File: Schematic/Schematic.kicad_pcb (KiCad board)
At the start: 2 copper layers, 115.1 x 171.2 mm, 126 parts, among them J1 HUB75_DATA, J10 Conn_01x03_Pin, J11 Conn_01x03_Pin, J12 Conn_01x03_Pin, J17 Conn_01x03_Pin, J18 LASER, J19 LDR, J2 KEYPAD, J20 WS2812B_DATA, J21 WS2812B_PWR, J3 HUB75_PWR, J4 AUDIO_OUT, J5 DEBUG_HEADER, J6 Conn_01x03_Pin, J7 Conn_01x03_Pin, J8 Conn_01x03_Pin, J9 Conn_01x03_Pin, SW1 RESET, U1 74LS08, U2 STM32F091RCT6, U3 LM386, U4 LM2678S-12, U5 LD1117S33TR_SOT223, U6 MAX7375AXR805, U7 LM358

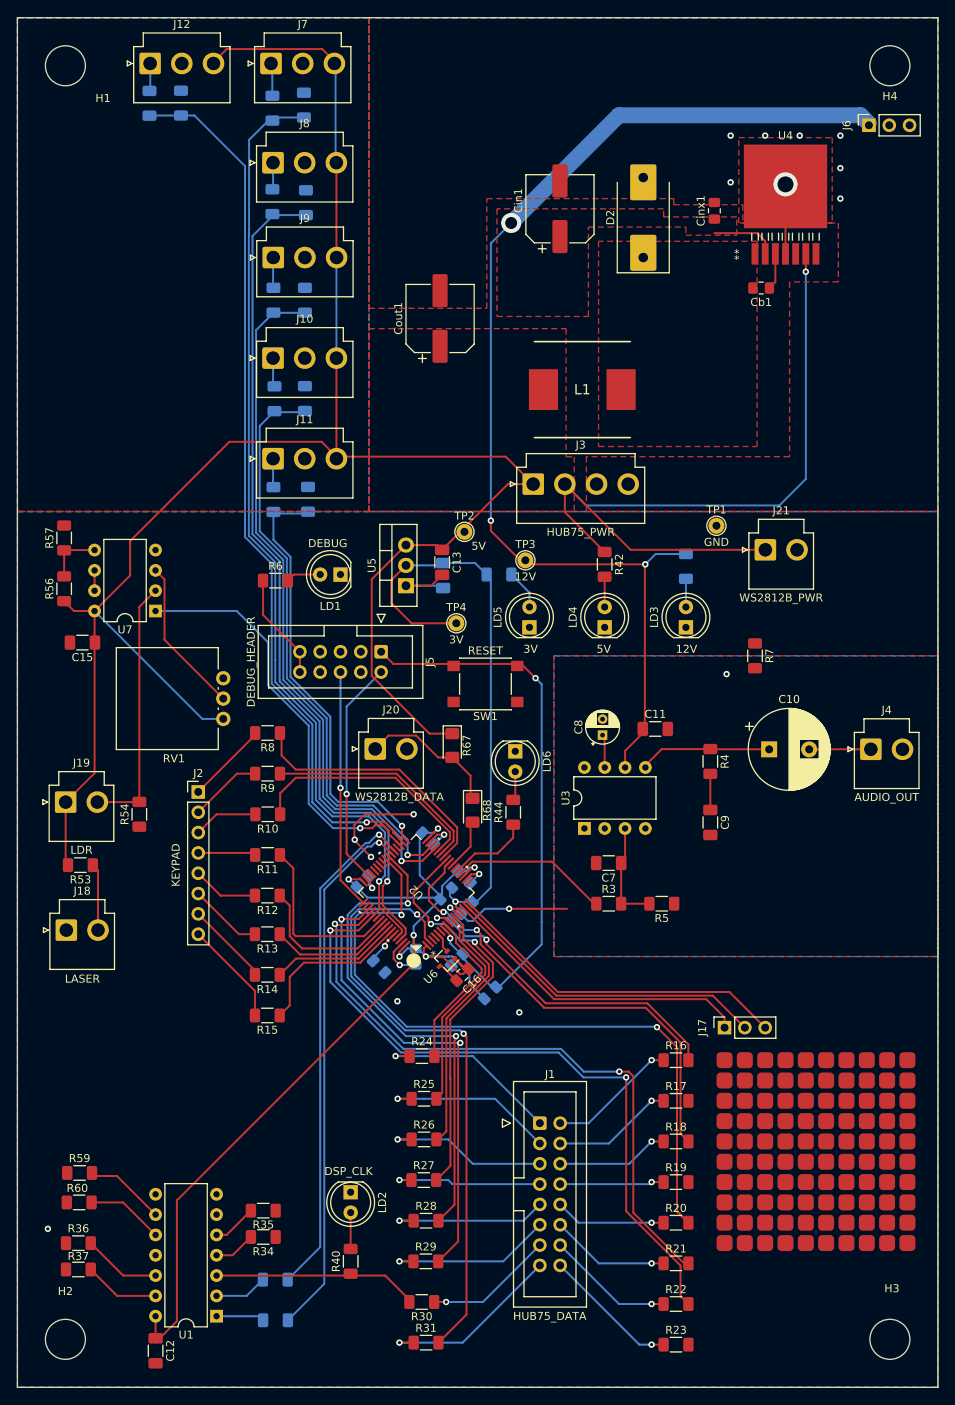
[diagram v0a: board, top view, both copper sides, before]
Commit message: fixed exporting script
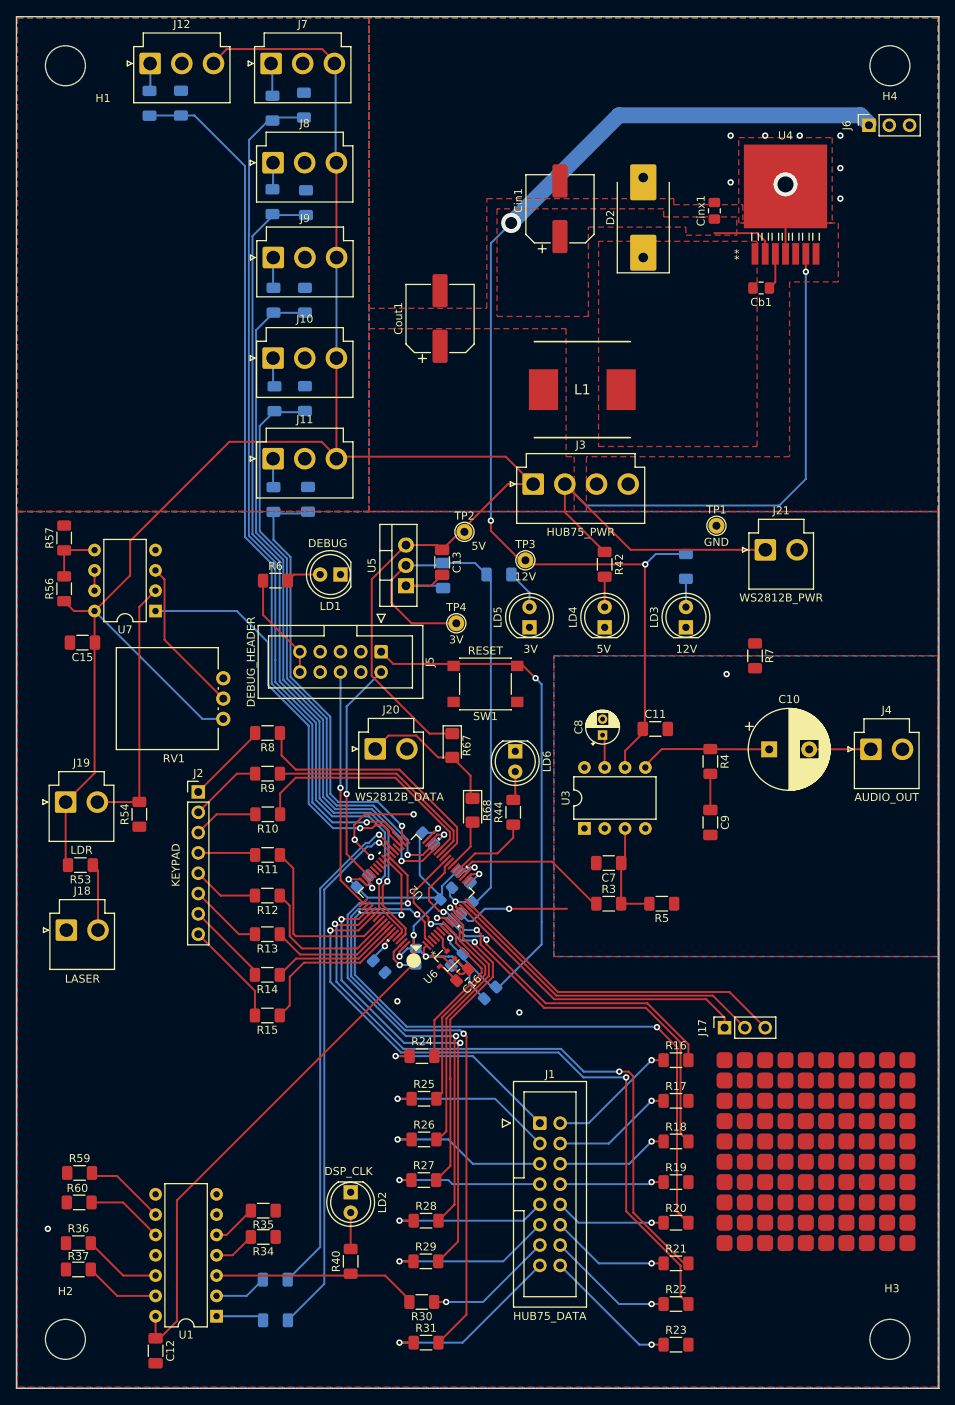
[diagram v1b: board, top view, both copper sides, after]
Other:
- board size 115.1 x 171.2 mm -> 115.3 x 171.4 mm
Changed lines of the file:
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@@
     (aux_axis_origin 35.941 23.622)
     (pcbplotparams
-      (layerselection 0x0011010_fffffffe)
+      (layerselection 0x0000000_fffffffe)
       (plot_on_all_layers_selection 0x0011010_80000000)
       (disableapertmacros false)
@@
       (plotreference true)
       (plotvalue true)
-      (plotinvisibletext false)
+      (plotinvisibletext true)
       (sketchpadsonfab false)
       (subtractmaskfromsilk false)
@@
   (gr_circle (center 151.003 23.622) (end 151.003 23.622)
     (stroke (width 0.15) (type default)) (fill none) (layer "Dwgs.User"))
-  (gr_circle (center 35.941 23.622) (end 36.068 23.622)
+  (gr_circle (center 35.941 23.622) (end 35.941 23.622)
     (stroke (width 0.15) (type default)) (fill none) (layer "Dwgs.User"))
-  (gr_rect (start 35.941 23.622) (end 151.003 194.818)
+  (gr_rect (start 35.814 23.495) (end 151.13 194.945)
     (stroke (width 0.1) (type default)) (fill none) (layer "Edge.Cuts"))
   (gr_text "12V" (at 118.237 103.124) (layer "F.SilkS")

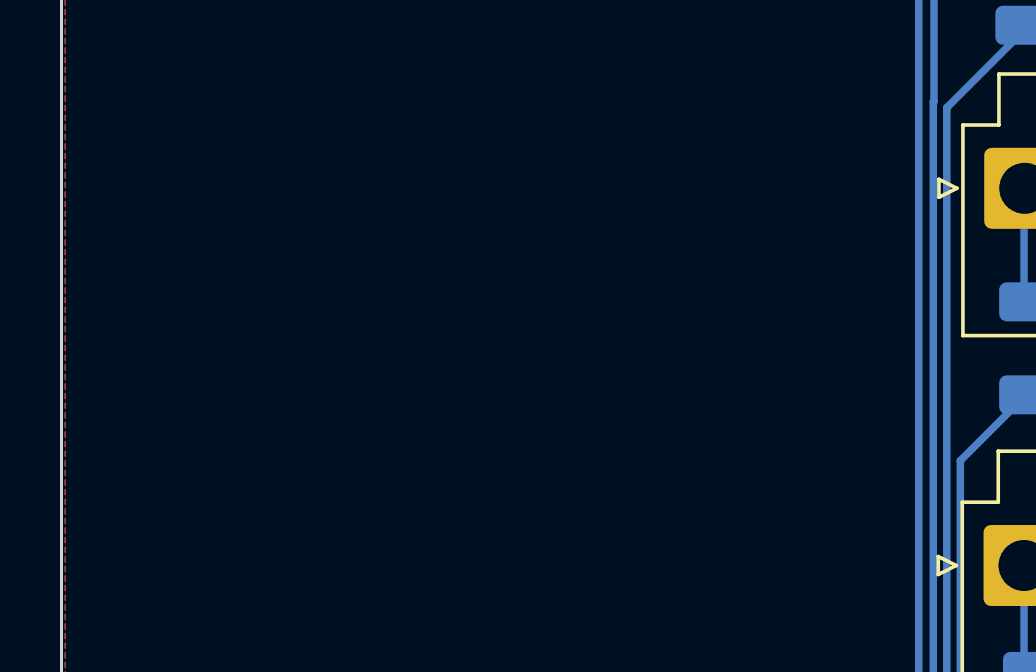
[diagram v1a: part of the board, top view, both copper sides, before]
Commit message: Updated svg's
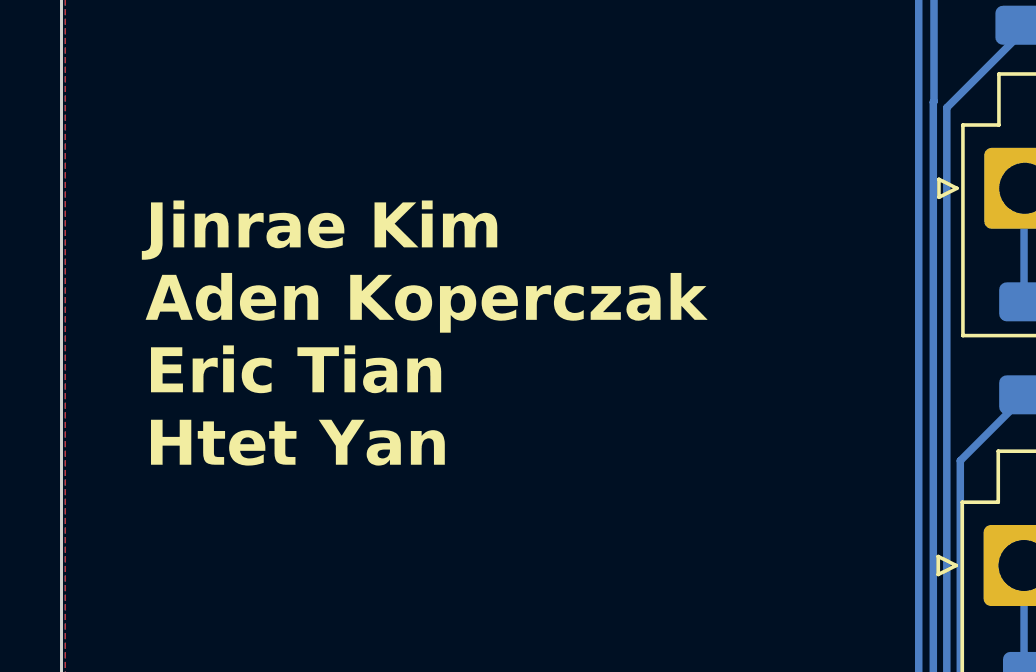
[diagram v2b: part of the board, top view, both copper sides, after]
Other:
- board text added: "Jinrae Kim​ Aden Koperczak​ Eric Tian​ Htet Yan​"
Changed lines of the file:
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@@
   (gr_rect (start 35.814 23.495) (end 151.13 194.945)
     (stroke (width 0.1) (type default)) (fill none) (layer "Edge.Cuts"))
+  (gr_text "Jinrae Kim​\nAden Koperczak​\nEric Tian​\nHtet Yan​" (at 38.608 62.992) (layer "F.SilkS")
+    (effects (font (size 1.5 1.5) (thickness 0.3) bold) (justify left bottom))
+  )
   (gr_text "12V" (at 118.237 103.124) (layer "F.SilkS")
     (effects (font (size 1 1) (thickness 0.15)) (justify left bottom))

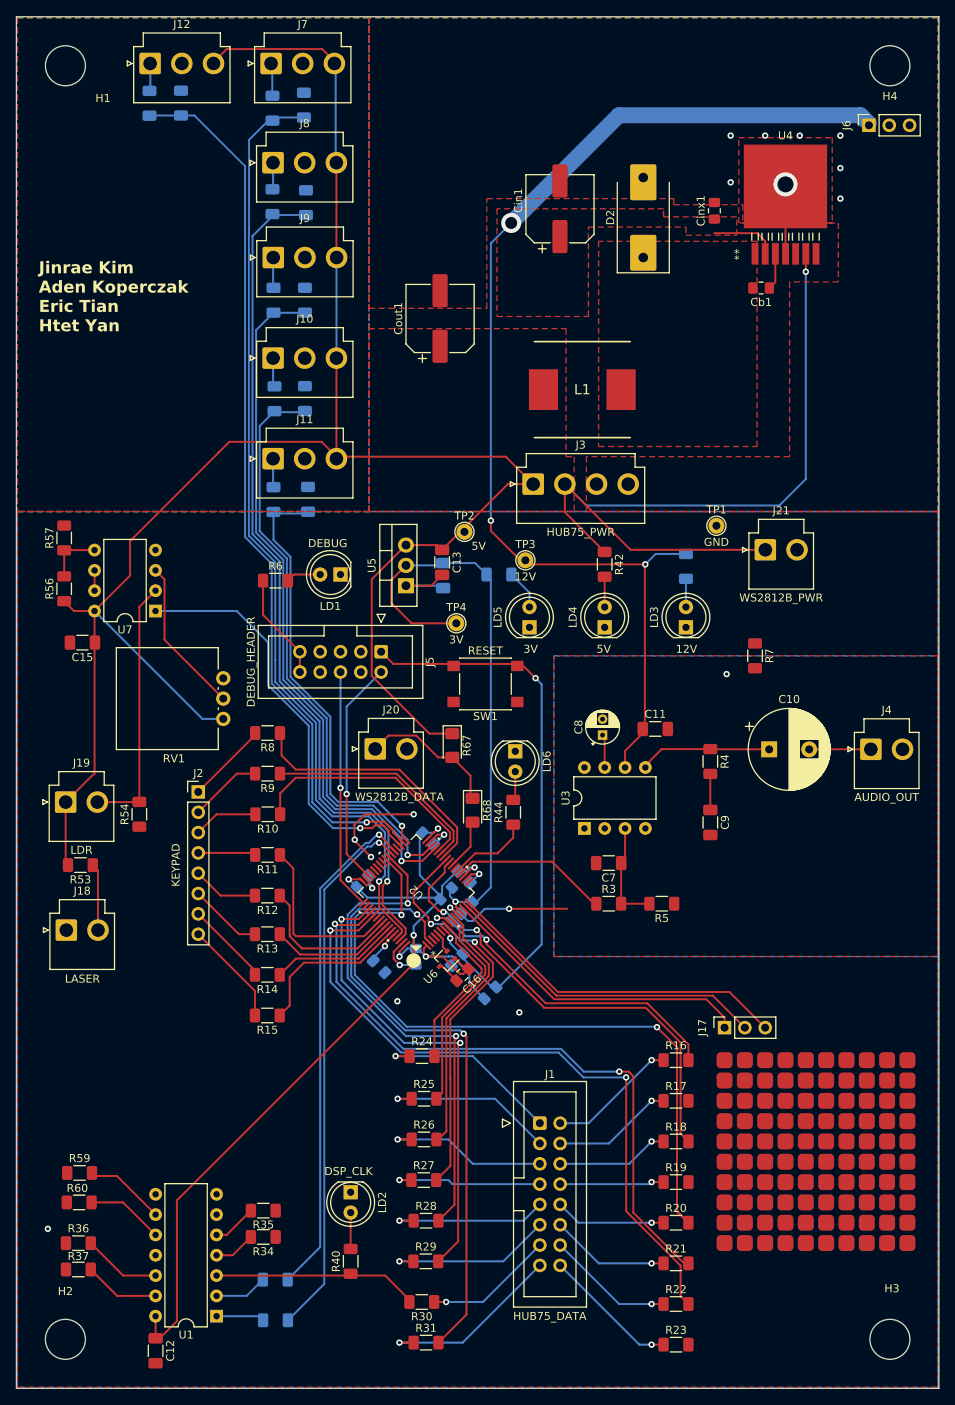
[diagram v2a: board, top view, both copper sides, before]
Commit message: Implemented some suggestions from presentation. Power trace size, reset button position, mounting holes, copper fill near edge, WS Data moved, removed debuge LED and analog vias.
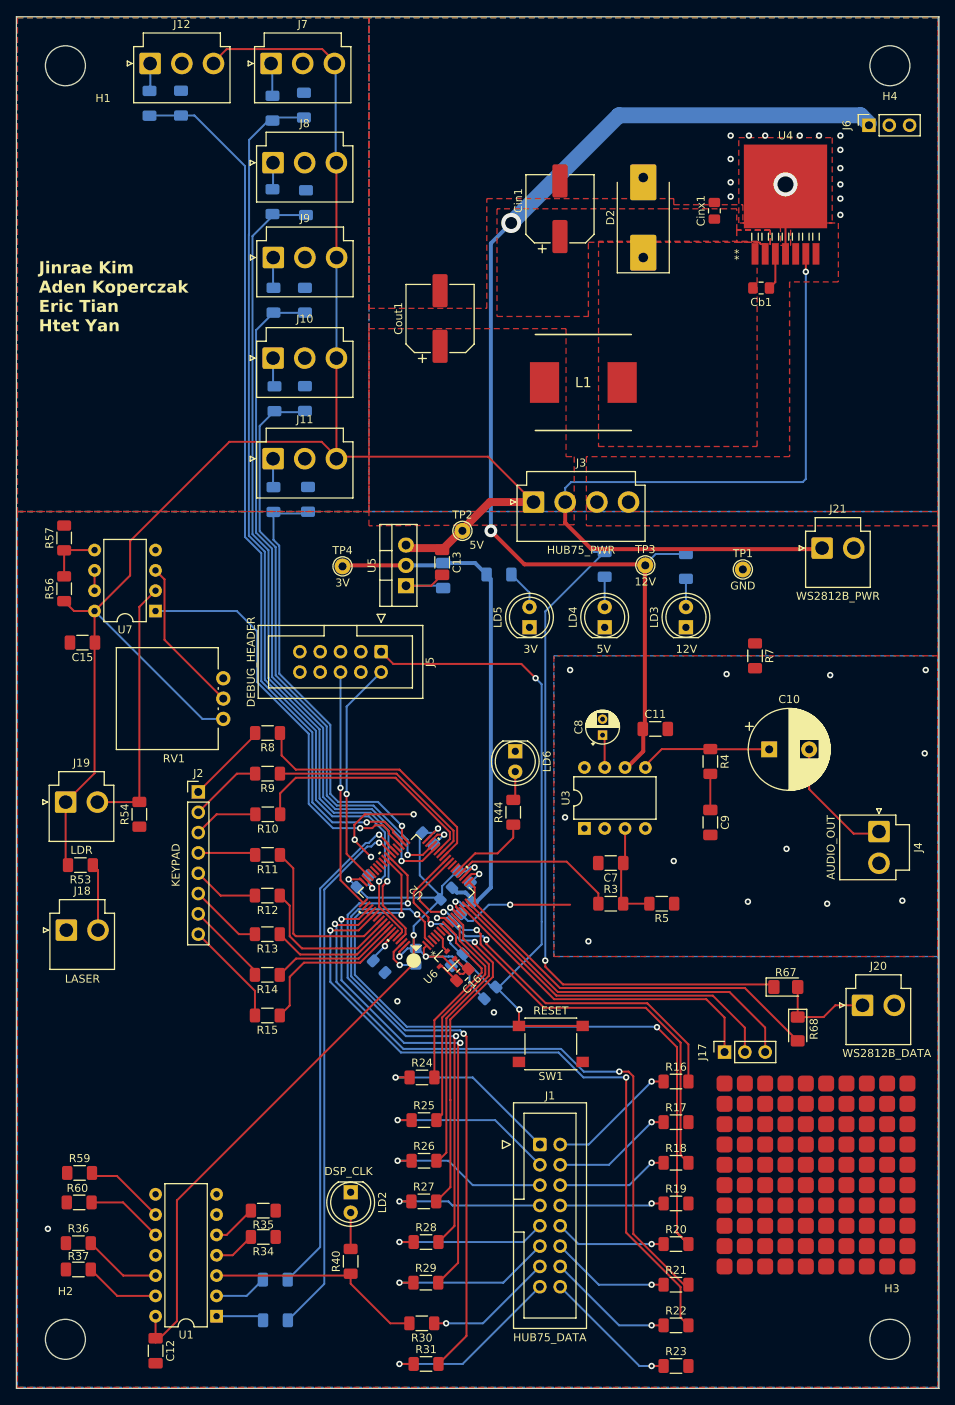
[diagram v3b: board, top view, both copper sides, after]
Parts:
- removed LD1: LED_Red, LED_THT:LED_D5.0mm
- removed R6: 10k, Resistor_SMD:R_1206_3216Metric_Pad1.30x1.75mm_HandSolder
- R42: moved to B.Cu
- moved J20 68.8 mm to (141.6, 147.1)
- moved R67 51.5 mm to (132.0, 144.8), turned to 0 degrees
- moved R68 49.0 mm to (133.5, 150.0)
- moved SW1 45.7 mm to (102.6, 151.9)
- moved TP4 15.9 mm to (76.6, 92.2)
- moved TP3 15.0 mm to (114.4, 92.1)
- moved J4 10.3 mm to (143.6, 125.3), turned to -90 degrees
- moved J21 7.09 mm to (136.5, 89.9)
- moved TP1 6.38 mm to (126.6, 92.6)
- moved J17 3.05 mm to (124.3, 152.9)
- moved REF** 2.92 mm to (124.3, 156.8)
- moved J1 2.67 mm to (101.2, 164.5)
- moved R16 2.67 mm to (118.3, 156.6)
- moved R17 2.67 mm to (118.3, 161.7)
- moved R18 2.67 mm to (118.3, 166.8)
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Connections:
- J5 pad 10: /microprocessor/U5V -> unconnected-(J5-Pin_10-Pad10)
- R68 pad 2: PA7 -> PA3
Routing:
- net +5V: track 343.6 -> 403.0 mm, vias 1 -> 2
- net PA3: track 0.00 -> 50.4 mm
- net /microprocessor/NRST: track 72.6 -> 86.7 mm, vias 2 -> 3
- net /microprocessor/U5V: track 13.3 -> 0.00 mm
- net +12V: track 151.7 -> 143.5 mm, vias 3 -> 2
- net Net-(J4-Pin_1): track 8.21 -> 15.2 mm
- net PA7: track 6.30 -> 0.00 mm
- net Net-(J20-Pin_1): track 17.5 -> 11.3 mm
- net Vin: track 74.2 -> 68.5 mm
- net Net-(LD1-A): track 4.35 -> 0.00 mm
- net PC4: track 58.2 -> 62.5 mm
- net PA2: track 43.5 -> 46.5 mm
- net PA1: track 41.1 -> 44.2 mm
- net PA0: track 39.5 -> 42.6 mm
- net PC5: track 50.8 -> 53.4 mm
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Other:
- board text removed: "DEBUG"

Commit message: Lab fixes
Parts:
- added C17: 10n, Capacitor_SMD:C_1206_3216Metric_Pad1.33x1.80mm_HandSolder, B.Cu at (60.6, 34.3)
- added C18: 10n, Capacitor_SMD:C_1206_3216Metric_Pad1.33x1.80mm_HandSolder, B.Cu at (76.3, 83.8)
- added C19: 10n, Capacitor_SMD:C_1206_3216Metric_Pad1.33x1.80mm_HandSolder, B.Cu at (75.7, 71.4)
- added C20: 10n, Capacitor_SMD:C_1206_3216Metric_Pad1.33x1.80mm_HandSolder, B.Cu at (75.7, 58.9)
- added C21: 10n, Capacitor_SMD:C_1206_3216Metric_Pad1.33x1.80mm_HandSolder, B.Cu at (75.7, 46.7)
- added C22: 10n, Capacitor_SMD:C_1206_3216Metric_Pad1.33x1.80mm_HandSolder, B.Cu at (75.7, 34.7)
- added J13: Conn_01x03_Pin, Connector_PinHeader_2.54mm:PinHeader_1x03_P2.54mm_Vertical, F.Cu at (72.4, 88.9)
- added R6: 10k, Resistor_SMD:R_1206_3216Metric_Pad1.30x1.75mm_HandSolder, B.Cu at (53.5, 139.8)
- added R61: 10k, Resistor_SMD:R_1206_3216Metric_Pad1.30x1.75mm_HandSolder, B.Cu at (53.5, 136.5)
- added R62: 10k, Resistor_SMD:R_1206_3216Metric_Pad1.30x1.75mm_HandSolder, B.Cu at (53.5, 133.2)
- added R63: 10k, Resistor_SMD:R_1206_3216Metric_Pad1.30x1.75mm_HandSolder, B.Cu at (53.5, 129.9)
- moved TP4 19.3 mm to (95.0, 97.9)
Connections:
- J10 pad 3: +5V -> /Sensors/Vsens
- J11 pad 3: +5V -> /Sensors/Vsens
- J12 pad 3: +5V -> /Sensors/Vsens
- J7 pad 3: +5V -> /Sensors/Vsens
- J8 pad 3: +5V -> /Sensors/Vsens
- J9 pad 3: +5V -> /Sensors/Vsens
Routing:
- net /Sensors/Vsens: track 0.00 -> 82.6 mm
- net +5V: track 403.0 -> 321.3 mm
- net +3V0: track 137.4 -> 180.2 mm
- net Vin: track 68.5 -> 61.0 mm
- net Net-(J2-Pin_8): track 13.1 -> 17.3 mm
- net PB12: track 54.9 -> 59.0 mm
- net PB11: track 73.8 -> 77.9 mm
- net PB8: track 119.1 -> 123.1 mm
- net Net-(J2-Pin_7): track 10.6 -> 14.4 mm
- net PB10: track 88.4 -> 92.2 mm
- net Net-(J2-Pin_5): track 8.24 -> 12.0 mm
- net PB9: track 107.0 -> 110.7 mm
- net Net-(J2-Pin_6): track 9.19 -> 12.7 mm
- net PB13: track 111.2 -> 112.8 mm
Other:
- board text added: "ECE477 Group 2 Skeeball Machine Main Board Jinrae Kim​ Aden Koperczak​ Eric Tian​ Htet Yan​ Revision 1.0 2023-10-18"
- board text removed: "Jinrae Kim​ Aden Koperczak​ Eric Tian​ Htet Yan​"

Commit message: Added level shifter (may or may not use) other minor fixes
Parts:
- removed J20: WS2812B_DATA, Connector_JST:JST_VH_B2P-VH-B_1x02_P3.96mm_Vertical
- removed J21: WS2812B_PWR, Connector_JST:JST_VH_B2P-VH-B_1x02_P3.96mm_Vertical
- removed R67: 7.5k, LED_SMD:LED_1206_3216Metric_Pad1.42x1.75mm_HandSolder
- removed R68: 3k, LED_SMD:LED_1206_3216Metric_Pad1.42x1.75mm_HandSolder
- added C23: 0.1u, Capacitor_SMD:C_1206_3216Metric_Pad1.33x1.80mm_HandSolder, B.Cu at (128.5, 164.3)
- added J14: WS2812B_DATA, Connector_JST:JST_VH_B2P-VH-B_1x02_P3.96mm_Vertical, F.Cu at (141.6, 147.1)
- added J15: WS2812B_PWR, Connector_JST:JST_VH_B2P-VH-B_1x02_P3.96mm_Vertical, F.Cu at (136.5, 89.9)
- added J16: Conn_01x03_Pin, Connector_PinHeader_2.54mm:PinHeader_1x03_P2.54mm_Vertical, F.Cu at (134.4, 159.8)
- added R64: 7.5k, LED_SMD:LED_1206_3216Metric_Pad1.42x1.75mm_HandSolder, F.Cu at (132.0, 144.8)
- added R65: 3k, LED_SMD:LED_1206_3216Metric_Pad1.42x1.75mm_HandSolder, F.Cu at (133.5, 150.0)
- added U8: SN74AHCT125N, SN74AHCT125:N14, F.Cu at (130.0, 174.5)
- J17: value Conn_01x03_Pin -> Conn_01x05_Pin; footprint Connector_PinSocket_2.54mm:PinSocket_1x03_P2.54mm_Vertical -> Connector_PinHeader_2.54mm:PinHeader_1x05_P2.54mm_Vertical
- moved REF** 84.4 mm to (40.6, 146.3)
- moved J17 56.0 mm to (68.3, 153.2), turned to 0 degrees
- moved C12 25.2 mm to (64.3, 167.6)
- moved SW1 5.64 mm to (108.0, 150.3)
- moved R24 4.45 mm to (86.3, 160.5)
- moved R16 3.68 mm to (118.4, 160.3)
- moved R32 3.18 mm to (67.3, 189.5)
- moved R33 3.17 mm to (67.3, 184.4)
- moved R25 2.93 mm to (86.6, 164.3)
- moved R17 2.41 mm to (118.3, 164.1)
- moved R26 1.41 mm to (86.6, 167.9)
- moved R18 1.14 mm to (118.3, 167.9)
- moved R34 0.25 mm to (66.7, 176.3)
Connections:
- J17 pad 1: PA0 -> +3V0
- J17 pad 2: PA1 -> PA0
- J17 pad 3: PA2 -> PA1
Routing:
- net +5V: track 321.3 -> 392.3 mm
- net PA3: track 50.4 -> 74.3 mm
- net PA2: track 46.5 -> 62.5 mm, vias 0 -> 2
- net Net-(J14-Pin_1): track 0.00 -> 15.0 mm
- net PA1: track 44.2 -> 59.2 mm, vias 0 -> 2
- net PA0: track 42.6 -> 57.4 mm, vias 0 -> 2
- net /WS2812B/WS_DATA_RES: track 0.00 -> 14.5 mm
- net Net-(J20-Pin_1): track 11.3 -> 0.00 mm
- net /WS2812B/WS_DATA_SHIFTER: track 0.00 -> 7.42 mm
- net PC11: track 83.9 -> 90.7 mm
- net PC12: track 88.9 -> 95.3 mm
- net PC6: track 63.5 -> 68.7 mm
- net PC7: track 67.1 -> 72.0 mm
- net PC1: track 44.7 -> 49.4 mm
- net PC0: track 23.2 -> 27.8 mm
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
